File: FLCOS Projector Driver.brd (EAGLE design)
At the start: 73.9 x 62.1 mm, 64 parts, among them IC2 LM3414, IC3 MIC5219BM5, IC4 MIC5219BM5, IC5 LM3414, IC6 LM3414, Q1 14.31818MHz, Q3 12MHz, T2 S8050, T3 S8050, U1 TVP5150-NTSC_DECODER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

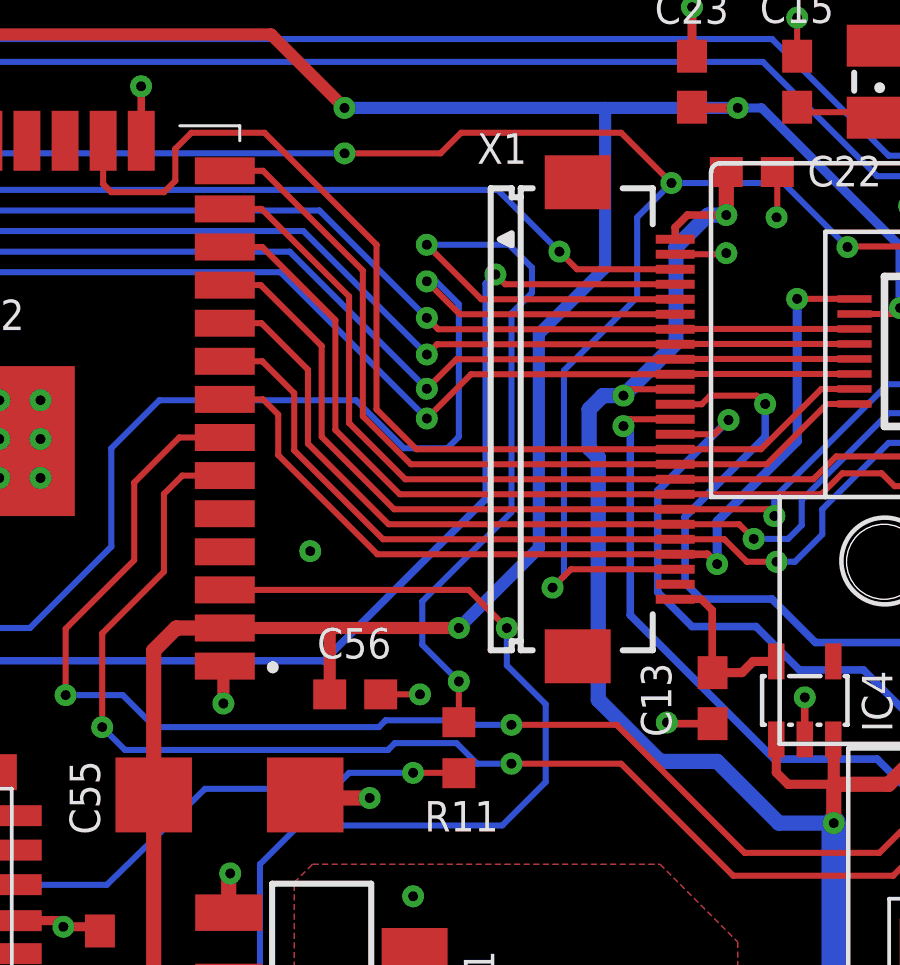
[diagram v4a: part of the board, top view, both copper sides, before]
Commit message: GPIO0 to reset the TVP, ESP_EN_N to reset the FLCOS
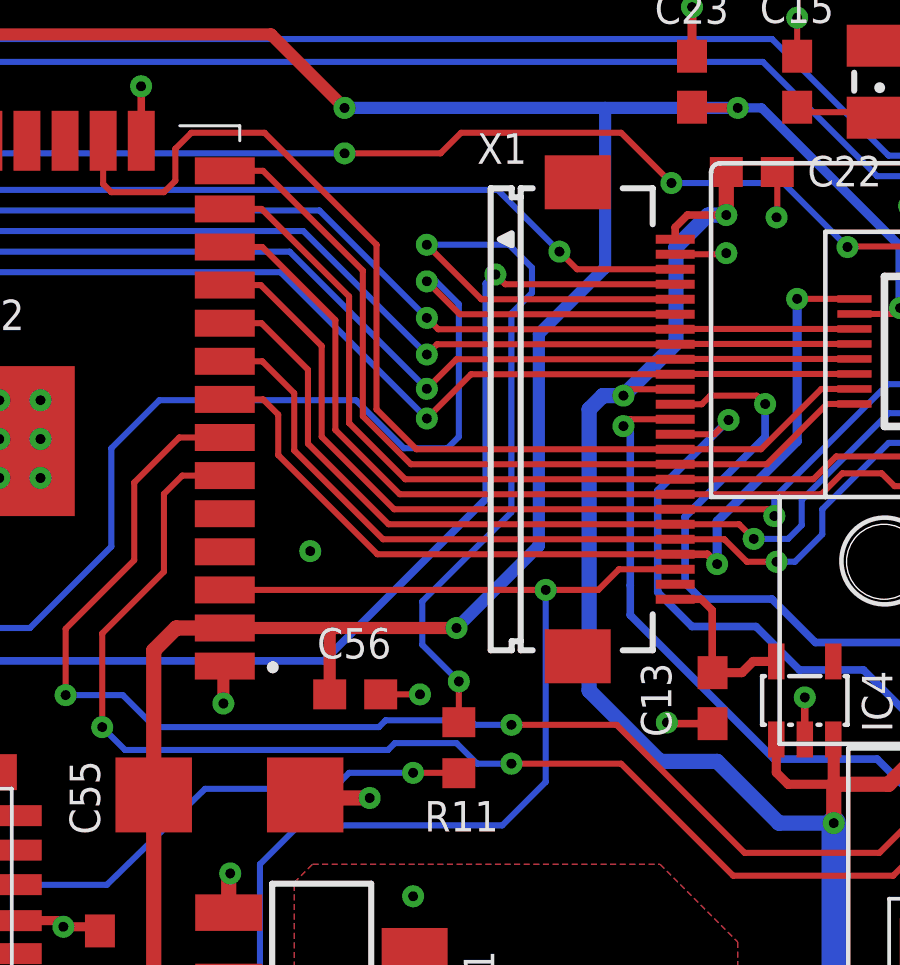
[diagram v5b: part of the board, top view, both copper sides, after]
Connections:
- net ESP_EN_N: now also X1.23
- net TVP_FL_RST_N: no longer X1.23
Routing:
- net TVP_FL_RST_N: track 111.4 -> 92.0 mm, vias 7 -> 6
- net ESP_EN_N: track 44.6 -> 50.7 mm
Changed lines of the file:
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@@
 <wire x1="39.0144" y1="15.411" x2="36.8232" y2="15.411" width="0.8128" layer="16"/>
 <wire x1="36.8232" y1="15.411" x2="36.8046" y2="15.3924" width="0.8128" layer="16"/>
-<wire x1="38.3286" y1="48.6918" x2="38.3286" y2="49.9872" width="0.508" layer="16"/>
 <wire x1="42.5958" y1="38.2524" x2="40.6908" y2="38.2524" width="0.508" layer="16"/>
 <wire x1="46.482" y1="29.8704" x2="46.482" y2="36.195" width="0.8128" layer="16"/>
@@
 <wire x1="42.5958" y1="38.2524" x2="44.6532" y2="36.195" width="0.508" layer="16"/>
 <wire x1="44.6532" y1="36.195" x2="46.482" y2="36.195" width="0.508" layer="16"/>
-<wire x1="38.6334" y1="40.3098" x2="40.6908" y2="38.2524" width="0.508" layer="16"/>
-<wire x1="38.3286" y1="48.6918" x2="38.6334" y2="48.387" width="0.508" layer="16"/>
-<wire x1="38.6334" y1="48.387" x2="38.6334" y2="40.3098" width="0.508" layer="16"/>
 <wire x1="38.3286" y1="49.9872" x2="38.7858" y2="50.4444" width="0.508" layer="16"/>
 <wire x1="38.7858" y1="50.4444" x2="39.4716" y2="50.4444" width="0.508" layer="16"/>
+<wire x1="40.6908" y1="38.2524" x2="38.3286" y2="40.6146" width="0.508" layer="16"/>
+<wire x1="38.3286" y1="40.6146" x2="38.3286" y2="49.9872" width="0.508" layer="16"/>
 </signal>
 <signal name="GND">
@@
 <wire x1="44.5008" y1="38.3286" x2="47.9298" y2="38.3286" width="0.254" layer="16"/>
 <wire x1="39.4716" y1="49.4284" x2="39.7002" y2="49.1998" width="0.254" layer="16"/>
-<wire x1="39.7002" y1="49.1998" x2="39.7002" y2="43.1292" width="0.254" layer="16"/>
+<wire x1="39.7002" y1="49.1998" x2="39.7002" y2="44.1198" width="0.254" layer="16"/>
+<wire x1="39.7002" y1="44.1198" x2="39.7002" y2="43.1292" width="0.254" layer="16"/>
 <wire x1="39.7002" y1="43.1292" x2="44.5008" y2="38.3286" width="0.254" layer="16"/>
 </signal>
@@
 <wire x1="33.8582" y1="23.872559375" x2="33.8582" y2="26.7208" width="0.2032" layer="1"/>
 <wire x1="33.8582" y1="26.7208" x2="32.5374" y2="28.0416" width="0.2032" layer="1"/>
-<via x="33.9852" y="42.6992" extent="1-16" drill="0.3302"/>
+<via x="33.909" y="42.6992" extent="1-16" drill="0.3302"/>
 <wire x1="38.862" y1="54.7116" x2="36.6522" y2="52.5018" width="0.4064" layer="16"/>
 <wire x1="26.184" y1="42.6992" x2="29.6418" y2="42.6992" width="0.4064" layer="1"/>
-<wire x1="29.6418" y1="42.6992" x2="33.9852" y2="42.6992" width="0.4064" layer="1"/>
+<wire x1="29.6418" y1="42.6992" x2="33.909" y2="42.6992" width="0.4064" layer="1"/>
 <wire x1="29.6808" y1="40.4876" x2="29.6808" y2="42.6602" width="0.4064" layer="1"/>
 <wire x1="29.6808" y1="42.6602" x2="29.6418" y2="42.6992" width="0.4064" layer="1"/>
@@
 <wire x1="27.7266" y1="62.484" x2="30.1752" y2="60.0354" width="0.4064" layer="1"/>
 <wire x1="17.7664" y1="62.484" x2="27.7266" y2="62.484" width="0.4064" layer="1"/>
-<wire x1="36.6522" y1="45.3662" x2="33.9852" y2="42.6992" width="0.4064" layer="16"/>
-<wire x1="36.6522" y1="52.5018" x2="36.6522" y2="45.3662" width="0.4064" layer="16"/>
+<wire x1="36.6522" y1="45.4424" x2="33.909" y2="42.6992" width="0.4064" layer="16"/>
+<wire x1="36.6522" y1="52.5018" x2="36.6522" y2="45.4424" width="0.4064" layer="16"/>
 </signal>
 <signal name="MOTOR">
@@
 <contactref element="R67" pad="1"/>
 <contactref element="T3" pad="3"/>
-<via x="35.5854" y="42.6974" extent="1-16" drill="0.3302"/>
+<via x="36.8808" y="43.9692" extent="1-16" drill="0.3302"/>
 <via x="31.6992" y="22.1742" extent="1-16" drill="0.3302"/>
 <wire x1="31.6722" y1="23.8878" x2="31.6664" y2="23.882" width="0.2032" layer="1"/>
@@
 <wire x1="26.2076" y1="43.9928" x2="26.184" y2="43.9692" width="0.2032" layer="1"/>
 <wire x1="28.6512" y1="36.1188" x2="35.433" y2="36.1188" width="0.2032" layer="16"/>
-<wire x1="34.3136" y1="43.9692" x2="35.5854" y2="42.6974" width="0.2032" layer="1"/>
-<wire x1="26.184" y1="43.9692" x2="34.3136" y2="43.9692" width="0.2032" layer="1"/>
 <wire x1="35.433" y1="36.1188" x2="36.8808" y2="37.5666" width="0.2032" layer="16"/>
-<wire x1="35.5854" y1="41.4528" x2="35.5854" y2="42.6974" width="0.2032" layer="16"/>
-<wire x1="36.8808" y1="37.5666" x2="36.8808" y2="40.1574" width="0.2032" layer="16"/>
-<wire x1="36.8808" y1="40.1574" x2="35.5854" y2="41.4528" width="0.2032" layer="16"/>
+<contactref element="X1" pad="23"/>
+<wire x1="41.1976" y1="44.657" x2="39.323" y2="44.657" width="0.2032" layer="1"/>
+<wire x1="39.323" y1="44.657" x2="38.6352" y2="43.9692" width="0.2032" layer="1"/>
+<wire x1="38.6352" y1="43.9692" x2="36.8808" y2="43.9692" width="0.2032" layer="1"/>
+<wire x1="36.8808" y1="37.5666" x2="36.8808" y2="43.9692" width="0.2032" layer="16"/>
+<wire x1="26.184" y1="43.9692" x2="36.8808" y2="43.9692" width="0.2032" layer="1"/>
 </signal>
 <signal name="N$16">
@@
 <signal name="TVP_FL_RST_N">
 <contactref element="U1" pad="8"/>
-<contactref element="X1" pad="23"/>
 <contactref element="T2" pad="3"/>
 <contactref element="U2" pad="25"/>
@@
 <wire x1="46.9392" y1="55.3974" x2="44.8056" y2="57.531" width="0.2032" layer="16"/>
 <wire x1="44.8056" y1="57.531" x2="41.0718" y2="57.531" width="0.2032" layer="16"/>
-<wire x1="41.0718" y1="57.531" x2="39.9288" y2="56.388" width="0.2032" layer="16"/>
-<wire x1="39.9288" y1="56.388" x2="39.9288" y2="53.721" width="0.2032" layer="16"/>
-<wire x1="39.9288" y1="53.721" x2="37.4904" y2="51.2826" width="0.2032" layer="16"/>
-<wire x1="37.4904" y1="44.4246" x2="37.1094" y2="44.0436" width="0.2032" layer="16"/>
-<via x="37.1094" y="44.0436" extent="1-16" drill="0.3302"/>
-<wire x1="37.1094" y1="44.0436" x2="37.7228" y2="44.657" width="0.2032" layer="1"/>
-<wire x1="37.7228" y1="44.657" x2="41.1976" y2="44.657" width="0.2032" layer="1"/>
-<wire x1="37.4904" y1="51.2826" x2="37.4904" y2="44.4246" width="0.2032" layer="16"/>
 <wire x1="9.184" y1="57.9392" x2="9.184" y2="59.1712" width="0.2032" layer="1"/>
 <wire x1="9.184" y1="59.1712" x2="9.2964" y2="59.2836" width="0.2032" layer="1"/>

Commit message: README update
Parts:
- added R12: 2K2, rcl:R0603
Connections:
- net FLCOS_D7: now also R12.2
- net GND: now also R12.1
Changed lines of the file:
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@@
 <attribute name="VALUE" x="12.1666" y="60.579" size="1.27" layer="27"/>
 </element>
+<element name="R12" library="rcl" package="R0603" value="2K2" x="-213.6648" y="-226.4664"/>
 </elements>
 <signals>
@@
 <wire x1="32.7152" y1="40.4876" x2="32.6898" y2="40.4876" width="0.2032" layer="1"/>
 <via x="32.6898" y="40.4876" extent="1-16" drill="0.3302"/>
+<contactref element="R12" pad="1"/>
+<wire x1="12.9822" y1="12.1158" x2="-214.5148" y2="-226.4664" width="0" layer="19" extent="1-1"/>
 </signal>
 <signal name="FLCOS_D7">
@@
 <wire x1="12.4206" y1="56.6166" x2="29.337" y2="56.6166" width="0.2032" layer="16"/>
 <wire x1="29.337" y1="56.6166" x2="32.9184" y2="53.0352" width="0.2032" layer="16"/>
+<contactref element="R12" pad="2"/>
+<wire x1="9.1858" y1="55.3974" x2="-212.8148" y2="-226.4664" width="0" layer="19" extent="1-1"/>
 </signal>
 <signal name="FLCOS_D6">

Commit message: Added pulldown on FL_D7, to set I2C Addr
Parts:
- moved R12 378.6 mm to (32.8, 60.9), turned to 270 degrees
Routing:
- net FLCOS_D7: track 40.1 -> 45.9 mm, vias 2 -> 3
- net GND: track 69.2 -> 70.7 mm, vias 62 -> 63
- net +5V: track 193.1 -> 194.0 mm
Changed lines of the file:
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@@
 <attribute name="MF" value="" x="37.9476" y="49.657" size="1.778" layer="27" rot="R270" display="off"/>
 <attribute name="MPN" value="" x="37.9476" y="49.657" size="1.778" layer="27" rot="R270" display="off"/>
-<attribute name="NAME" x="34.5934" y="58.1716" size="1.016" layer="25"/>
+<attribute name="NAME" x="34.6696" y="58.2478" size="1.016" layer="25"/>
 <attribute name="OC_FARNELL" value="unknown" x="37.9476" y="49.657" size="1.778" layer="27" rot="R270" display="off"/>
 <attribute name="OC_NEWARK" value="unknown" x="37.9476" y="49.657" size="1.778" layer="27" rot="R270" display="off"/>
@@
 <attribute name="VALUE" x="12.1666" y="60.579" size="1.27" layer="27"/>
 </element>
-<element name="R12" library="rcl" package="R0603" value="2K2" x="-213.6648" y="-226.4664"/>
+<element name="R12" library="rcl" package="R0603" value="2K2" x="32.766" y="60.9092" smashed="yes" rot="R270">
+<attribute name="NAME" x="31.5214" y="62.7634" size="1.016" layer="25"/>
+<attribute name="VALUE" x="30.861" y="61.5442" size="1.27" layer="27" rot="R270"/>
+</element>
 </elements>
 <signals>
@@
 <wire x1="15.5702" y1="16.9164" x2="16.8232" y2="18.1694" width="0.508" layer="1"/>
 <wire x1="16.8232" y1="18.1694" x2="19.564" y2="18.1694" width="0.508" layer="1"/>
-<wire x1="41.1976" y1="50.657" x2="39.6842" y2="50.657" width="0.2032" layer="1"/>
-<wire x1="39.6842" y1="50.657" x2="39.4716" y2="50.4444" width="0.2032" layer="1"/>
-<via x="39.4716" y="50.4444" extent="1-16" drill="0.3302"/>
+<via x="38.3286" y="50.0634" extent="1-16" drill="0.3302"/>
 <wire x1="54.5592" y1="40.8432" x2="56.007" y2="40.8432" width="0.3048" layer="1"/>
 <wire x1="56.3982" y1="41.2344" x2="56.3982" y2="42.3625" width="0.3048" layer="1"/>
@@
 <wire x1="46.482" y1="37.4904" x2="46.482" y2="36.195" width="0.508" layer="1"/>
 <via x="42.9006" y="56.4642" extent="1-16" drill="0.3302"/>
-<wire x1="39.4716" y1="50.4444" x2="41.2242" y2="52.197" width="0.508" layer="16"/>
 <wire x1="42.9006" y1="56.4642" x2="42.9006" y2="57.8984" width="0.508" layer="1"/>
 <wire x1="42.291" y1="56.4642" x2="42.9006" y2="56.4642" width="0.508" layer="16"/>
-<wire x1="41.2242" y1="52.197" x2="41.2242" y2="55.3974" width="0.508" layer="16"/>
+<wire x1="41.2242" y1="55.3974" x2="41.2242" y2="52.959" width="0.508" layer="16"/>
 <wire x1="41.2242" y1="55.3974" x2="42.291" y2="56.4642" width="0.508" layer="16"/>
 <wire x1="41.1976" y1="55.657" x2="41.1976" y2="56.0566" width="0.254" layer="1"/>
@@
 <wire x1="42.5958" y1="38.2524" x2="44.6532" y2="36.195" width="0.508" layer="16"/>
 <wire x1="44.6532" y1="36.195" x2="46.482" y2="36.195" width="0.508" layer="16"/>
-<wire x1="38.3286" y1="49.9872" x2="38.7858" y2="50.4444" width="0.508" layer="16"/>
-<wire x1="38.7858" y1="50.4444" x2="39.4716" y2="50.4444" width="0.508" layer="16"/>
 <wire x1="40.6908" y1="38.2524" x2="38.3286" y2="40.6146" width="0.508" layer="16"/>
-<wire x1="38.3286" y1="40.6146" x2="38.3286" y2="49.9872" width="0.508" layer="16"/>
+<wire x1="38.3286" y1="40.6146" x2="38.3286" y2="50.0634" width="0.508" layer="16"/>
+<wire x1="41.1976" y1="50.657" x2="38.9222" y2="50.657" width="0.2032" layer="1"/>
+<wire x1="38.9222" y1="50.657" x2="38.3286" y2="50.0634" width="0.2032" layer="1"/>
+<wire x1="41.2242" y1="52.959" x2="38.3286" y2="50.0634" width="0.508" layer="16"/>
 </signal>
 <signal name="GND">
@@
 <via x="32.6898" y="40.4876" extent="1-16" drill="0.3302"/>
 <contactref element="R12" pad="1"/>
-<wire x1="12.9822" y1="12.1158" x2="-214.5148" y2="-226.4664" width="0" layer="19" extent="1-1"/>
+<wire x1="32.766" y1="61.7592" x2="32.766" y2="63.3222" width="0.2032" layer="1"/>
+<via x="32.766" y="63.3222" extent="1-16" drill="0.3302"/>
 </signal>
 <signal name="FLCOS_D7">
@@
 <wire x1="11.2014" y1="55.3974" x2="12.4206" y2="56.6166" width="0.2032" layer="16"/>
 <wire x1="12.4206" y1="56.6166" x2="29.337" y2="56.6166" width="0.2032" layer="16"/>
-<wire x1="29.337" y1="56.6166" x2="32.9184" y2="53.0352" width="0.2032" layer="16"/>
+<wire x1="29.337" y1="56.6166" x2="30.7848" y2="55.1688" width="0.2032" layer="16"/>
 <contactref element="R12" pad="2"/>
-<wire x1="9.1858" y1="55.3974" x2="-212.8148" y2="-226.4664" width="0" layer="19" extent="1-1"/>
+<wire x1="30.7848" y1="55.1688" x2="32.9184" y2="53.0352" width="0.2032" layer="16"/>
+<wire x1="32.766" y1="60.0592" x2="32.766" y2="57.15" width="0.2032" layer="1"/>
+<wire x1="32.766" y1="57.15" x2="31.9278" y2="56.3118" width="0.2032" layer="1"/>
+<via x="31.9278" y="56.3118" extent="1-16" drill="0.3302"/>
+<wire x1="31.9278" y1="56.3118" x2="30.7848" y2="55.1688" width="0.2032" layer="16"/>
 </signal>
 <signal name="FLCOS_D6">
@@
 <signal name="GRN_PWM">
 <contactref element="X1" pad="13"/>
-<via x="39.4716" y="49.4284" extent="1-16" drill="0.3302"/>
-<wire x1="41.1976" y1="49.657" x2="39.7002" y2="49.657" width="0.2032" layer="1"/>
-<wire x1="39.7002" y1="49.657" x2="39.4716" y2="49.4284" width="0.2032" layer="1"/>
+<via x="39.624" y="49.657" extent="1-16" drill="0.3302"/>
+<wire x1="41.1976" y1="49.657" x2="39.624" y2="49.657" width="0.2032" layer="1"/>
 <contactref element="IC6" pad="6"/>
 <wire x1="61.7601" y1="22.0218" x2="60.4266" y2="22.0218" width="0.4064" layer="1"/>
@@
 <wire x1="56.8452" y1="29.4132" x2="47.9298" y2="38.3286" width="0.254" layer="16"/>
 <wire x1="44.5008" y1="38.3286" x2="47.9298" y2="38.3286" width="0.254" layer="16"/>
-<wire x1="39.4716" y1="49.4284" x2="39.7002" y2="49.1998" width="0.254" layer="16"/>
-<wire x1="39.7002" y1="49.1998" x2="39.7002" y2="44.1198" width="0.254" layer="16"/>
-<wire x1="39.7002" y1="44.1198" x2="39.7002" y2="43.1292" width="0.254" layer="16"/>
+<wire x1="39.624" y1="49.657" x2="39.7002" y2="49.5808" width="0.254" layer="16"/>
+<wire x1="39.7002" y1="49.5808" x2="39.7002" y2="43.1292" width="0.254" layer="16"/>
 <wire x1="39.7002" y1="43.1292" x2="44.5008" y2="38.3286" width="0.254" layer="16"/>
 </signal>
@@
 <wire x1="33.8582" y1="26.7208" x2="32.5374" y2="28.0416" width="0.2032" layer="1"/>
 <via x="33.909" y="42.6992" extent="1-16" drill="0.3302"/>
-<wire x1="38.862" y1="54.7116" x2="36.6522" y2="52.5018" width="0.4064" layer="16"/>
+<wire x1="36.6522" y1="52.5018" x2="38.862" y2="54.7116" width="0.4064" layer="16"/>
 <wire x1="26.184" y1="42.6992" x2="29.6418" y2="42.6992" width="0.4064" layer="1"/>
 <wire x1="29.6418" y1="42.6992" x2="33.909" y2="42.6992" width="0.4064" layer="1"/>
@@
 <via x="30.1752" y="60.0354" extent="1-16" drill="0.3302"/>
 <wire x1="43.2816" y1="60.0354" x2="38.862" y2="60.0354" width="0.4064" layer="16"/>
-<wire x1="38.862" y1="60.0354" x2="30.1752" y2="60.0354" width="0.4064" layer="16"/>
-<wire x1="38.862" y1="54.7116" x2="38.862" y2="60.0354" width="0.4064" layer="16"/>
+<wire x1="38.862" y1="60.0354" x2="32.5374" y2="60.0354" width="0.4064" layer="16"/>
+<wire x1="32.5374" y1="60.0354" x2="30.1752" y2="60.0354" width="0.4064" layer="16"/>
 <wire x1="27.7266" y1="62.484" x2="30.1752" y2="60.0354" width="0.4064" layer="1"/>
 <wire x1="17.7664" y1="62.484" x2="27.7266" y2="62.484" width="0.4064" layer="1"/>
 <wire x1="36.6522" y1="45.4424" x2="33.909" y2="42.6992" width="0.4064" layer="16"/>
 <wire x1="36.6522" y1="52.5018" x2="36.6522" y2="45.4424" width="0.4064" layer="16"/>
+<wire x1="38.862" y1="54.7116" x2="38.862" y2="60.0354" width="0.4064" layer="16"/>
 </signal>
 <signal name="MOTOR">
@@
 <wire x1="9.184" y1="59.1712" x2="9.2964" y2="59.2836" width="0.2032" layer="1"/>
 <via x="9.2964" y="59.2836" extent="1-16" drill="0.3302"/>
-<via x="30.1752" y="58.5216" extent="1-16" drill="0.3302"/>
+<via x="33.8328" y="58.5216" extent="1-16" drill="0.3302"/>
 <wire x1="41.0718" y1="57.531" x2="39.3954" y2="59.2074" width="0.2032" layer="1"/>
 <via x="41.0718" y="57.531" extent="1-16" drill="0.3302"/>
-<wire x1="30.1752" y1="58.5216" x2="10.0584" y2="58.5216" width="0.2032" layer="16"/>
+<wire x1="33.8328" y1="58.5216" x2="10.0584" y2="58.5216" width="0.2032" layer="16"/>
 <wire x1="10.0584" y1="58.5216" x2="9.2964" y2="59.2836" width="0.2032" layer="16"/>
-<wire x1="39.3954" y1="59.2074" x2="34.0614" y2="59.2074" width="0.2032" layer="1"/>
-<wire x1="33.3756" y1="58.5216" x2="30.1752" y2="58.5216" width="0.2032" layer="1"/>
-<wire x1="34.0614" y1="59.2074" x2="33.3756" y2="58.5216" width="0.2032" layer="1"/>
+<wire x1="39.3954" y1="59.2074" x2="34.5186" y2="59.2074" width="0.2032" layer="1"/>
+<wire x1="34.5186" y1="59.2074" x2="33.8328" y2="58.5216" width="0.2032" layer="1"/>
 </signal>
 </signals>
